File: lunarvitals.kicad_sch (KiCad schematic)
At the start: 40 parts, among them J1 ConductiveCord, J2 MPU6050, J3 SEN11574, J4 MAX30102, J5 USB_C_Receptacle_PowerOnly_6P, J6 Battery, J7 Conn_01x07, Q1 FS8205, SW1 SW_SPDT, U1 NRF52840-DONGLE, U3 AP2112K-3.3, U4 TP4056, U5 MLX90614ESF-AAA-000-TU, U6 DW01A

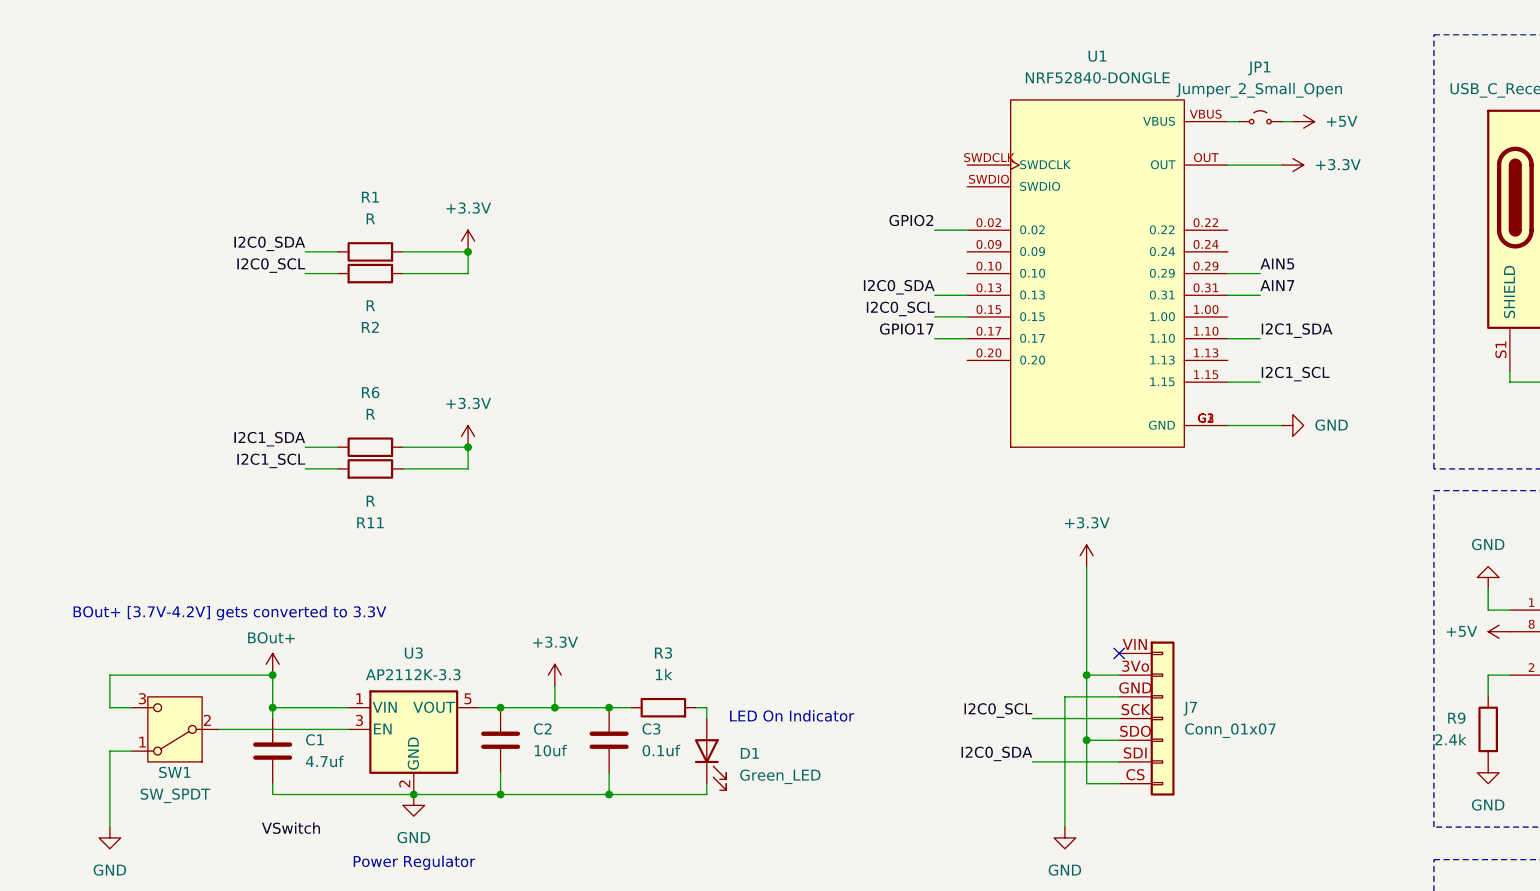
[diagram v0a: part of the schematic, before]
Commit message: solder jumper pads in case of problems with various parts of the circuit
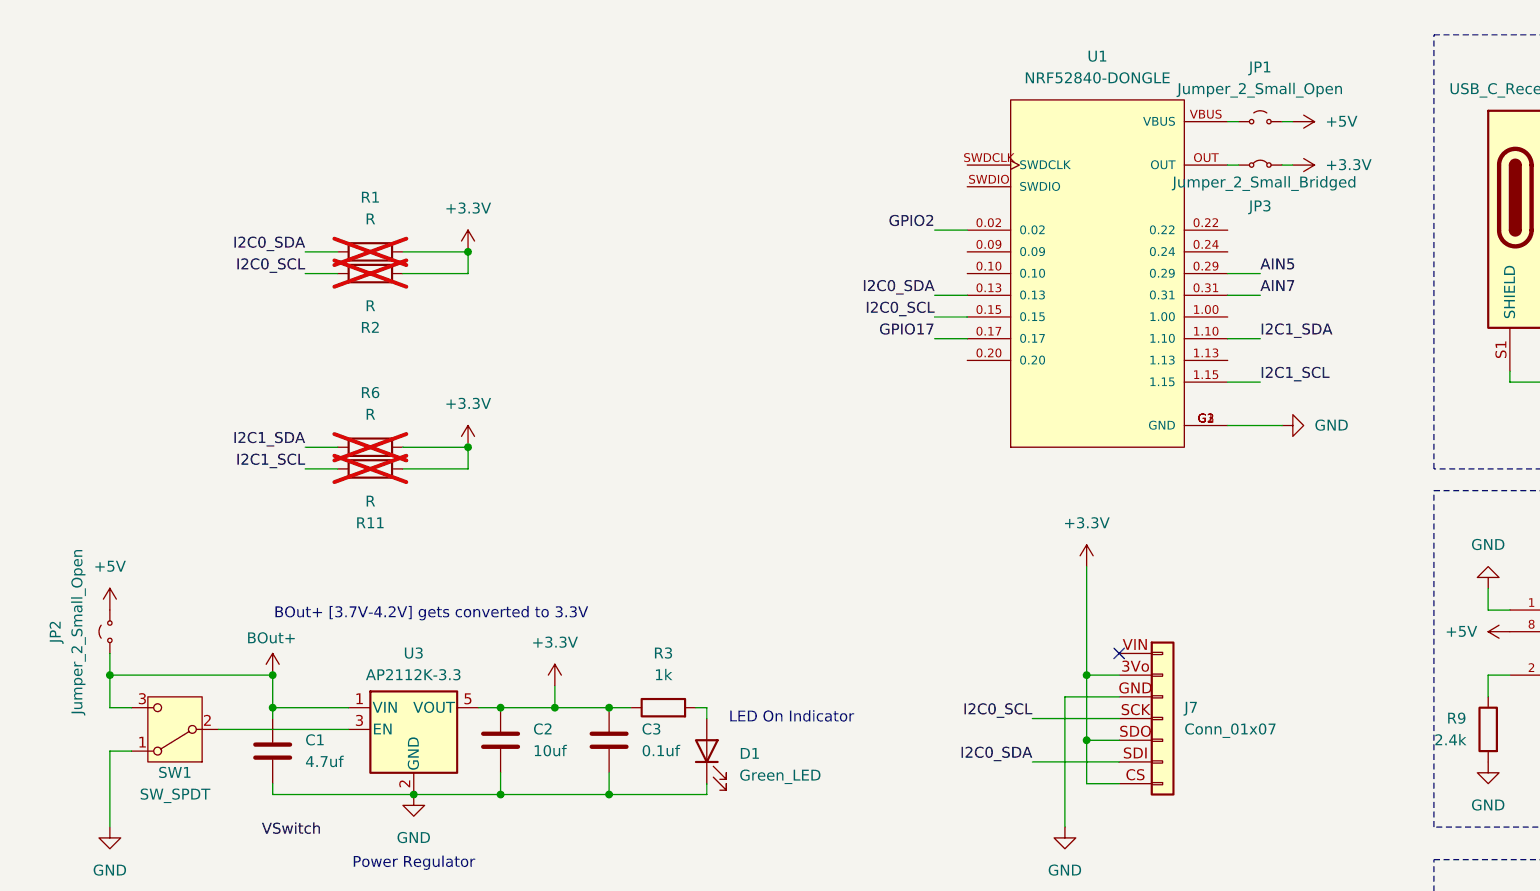
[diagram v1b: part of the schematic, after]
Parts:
- added JP2: Jumper_2_Small_Open, Jumper:SolderJumper-2_P1.3mm_Open_RoundedPad1.0x1.5mm, symbol Jumper:Jumper_2_Small_Open
- added JP3: Jumper_2_Small_Bridged, Jumper:SolderJumper-2_P1.3mm_Bridged_RoundedPad1.0x1.5mm, symbol Jumper:Jumper_2_Small_Bridged
- D1, D2, J7, JP1, U5: now left out of the parts list
- R1, R11, R2, R6: now not fitted; now left out of the parts list
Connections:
- net +3.3V: now also JP3.2 (B); no longer U1.OUT
- net +5V: now also JP2.2 (B)
- net BOut+: now also JP2.1 (A)
- new net: JP3.1 (A), U1.OUT

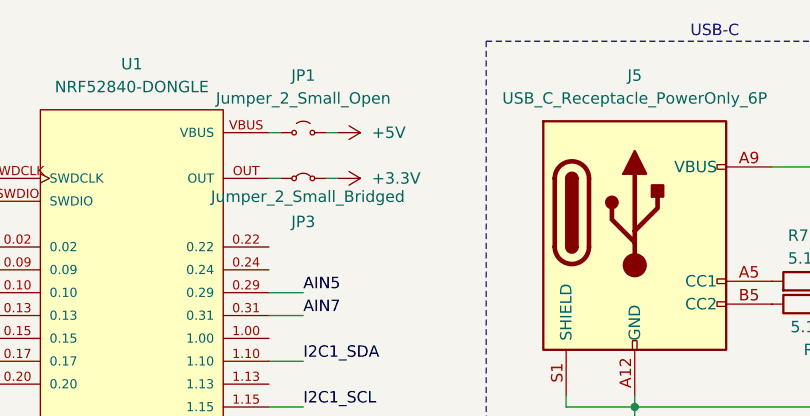
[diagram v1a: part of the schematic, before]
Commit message: fix contingency solder jumper connection
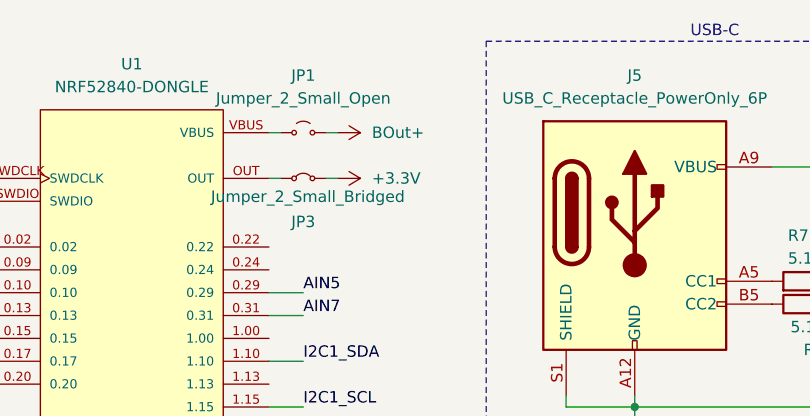
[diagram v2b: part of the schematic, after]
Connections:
- net +5V: no longer JP1.2 (B)
- net BOut+: now also JP1.2 (B)
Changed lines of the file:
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@@
 	)
 	(symbol
+		(lib_id "power:+3.3V")
+		(at 161.29 35.56 270)
+		(unit 1)
+		(exclude_from_sim no)
+		(in_bom yes)
+		(on_board yes)
+		(dnp no)
+		(property "Reference" "#PWR02"
+			(at 157.48 35.56 0)
+			(effects
+				(font
+					(size 1.27 1.27)
+				)
+				(hide yes)
+			)
+		)
+		(property "Value" "BOut+"
+			(at 165.1 35.56 90)
+			(effects
+				(font
+					(size 1.27 1.27)
+				)
+				(justify left)
+			)
+		)
+		(property "Footprint" ""
+			(at 161.29 35.56 0)
+			(effects
+				(font
+					(size 1.27 1.27)
+				)
+				(hide yes)
+			)
+		)
+		(property "Datasheet" ""
+			(at 161.29 35.56 0)
+			(effects
+				(font
+					(size 1.27 1.27)
+				)
+				(hide yes)
+			)
+		)
+		(property "Description" "Power symbol creates a global label with name \"+3.3V\""
+			(at 161.29 35.56 0)
+			(effects
+				(font
+					(size 1.27 1.27)
+				)
+				(hide yes)
+			)
+		)
+		(pin "1"
+		)
+		(instances
+			(project "lunarvitals"
+				(path "/5743f844-2fd9-4187-922b-f2fa73d8e73e"
+					(reference "#PWR02")
+					(unit 1)
+				)
+			)
+		)
+	)
+	(symbol
 		(lib_id "power:GND")
 		(at 58.42 165.1 90)
@@
 					(unit 1)
 				)
-			)
-		)
-	)
-	(symbol
-		(lib_id "power:+3.3V")
-		(at 161.29 35.56 270)
-		(unit 1)
-		(exclude_from_sim no)
-		(in_bom yes)
-		(on_board yes)
-		(dnp no)
-		(fields_autoplaced yes)
-		(property "Reference" "#PWR02"
-			(at 157.48 35.56 0)
-			(effects
-				(font
-					(size 1.27 1.27)
-				)
-				(hide yes)
-			)
-		)
-		(property "Value" "+5V"
-			(at 165.1 35.5599 90)
-			(effects
-				(font
-					(size 1.27 1.27)
-				)
-				(justify left)
-			)
-		)
-		(property "Footprint" ""
-			(at 161.29 35.56 0)
-			(effects
-				(font
-					(size 1.27 1.27)
-				)
-				(hide yes)
-			)
-		)
-		(property "Datasheet" ""
-			(at 161.29 35.56 0)
-			(effects
-				(font
-					(size 1.27 1.27)
-				)
-				(hide yes)
-			)
-		)
-		(property "Description" "Power symbol creates a global label with name \"+3.3V\""
-			(at 161.29 35.56 0)
-			(effects
-				(font
-					(size 1.27 1.27)
-				)
-				(hide yes)
-			)
-		)
-		(pin "1"
-		)
-		(instances
-			(project "lunarvitals"
-				(path "/5743f844-2fd9-4187-922b-f2fa73d8e73e"
-					(reference "#PWR02")
-					(unit 1)
-				)

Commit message: fix silkscreen, exclude from POS attributes
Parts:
- D3: footprint lunar_vitals_custom:KB APBA3010SURKCGKC-GX -> LED_SMD:LED_Kingbright_KPA-3010_3x2x1mm
- Q1: footprint FS8205A:SOT95P280X145-6N -> Package_TO_SOT_SMD:SOT-23-6
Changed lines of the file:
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@@
 			)
 		)
-		(property "Footprint" "lunar_vitals_custom:KB APBA3010SURKCGKC-GX"
+		(property "Footprint" "LED_SMD:LED_Kingbright_KPA-3010_3x2x1mm"
 			(at 241.3 96.52 0)
 			(effects
@@
 			)
 		)
-		(property "Footprint" "FS8205A:SOT95P280X145-6N"
+		(property "Footprint" "Package_TO_SOT_SMD:SOT-23-6"
 			(at 224.79 156.21 0)
 			(effects

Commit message: fix LED footprint
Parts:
- D3: footprint LED_SMD:LED_Kingbright_KPA-3010_3x2x1mm -> lunar_vitals_custom:LED_Kingbright_APBA3010SURKCGKC-GX_3x2x1mm
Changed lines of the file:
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@@
 			)
 		)
-		(property "Footprint" "LED_SMD:LED_Kingbright_KPA-3010_3x2x1mm"
+		(property "Footprint" "lunar_vitals_custom:LED_Kingbright_APBA3010SURKCGKC-GX_3x2x1mm"
 			(at 241.3 96.52 0)
 			(effects
